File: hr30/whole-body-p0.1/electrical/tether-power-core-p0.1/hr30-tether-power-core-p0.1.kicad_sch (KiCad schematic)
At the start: 0 parts

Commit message: Complete HR-30 safety and clean-build package
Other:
- sheet 03 Two series GV121CAC contactors and feedback loop renamed 03 Two series LC1D40ABD contactors and mirror-feedback loop
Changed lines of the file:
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@@
           (exclude_from_sim no) (in_bom yes) (on_board yes) (dnp no)
           (stroke (width 0.5) (type solid)) (fill (color 0 0 0 0.0000))
-          (property "Sheetname" "03 Two series GV121CAC contactors and feedback loop" (at 284.48 52.16 0) (effects (font (size 1.80 1.80)) (justify left bottom)))
+          (property "Sheetname" "03 Two series LC1D40ABD contactors and mirror-feedback loop" (at 284.48 52.16 0) (effects (font (size 1.80 1.80)) (justify left bottom)))
           (property "Sheetfile" "03_redundant_dc_interruption.kicad_sch" (at 284.48 67.40 0) (effects (font (size 1.50 1.50)) (justify left top)))
           (instances (project "hr30-tether-power-core-p0.1" (path "/ea4c0501-f5a0-52a4-9cf3-7c311b7f38a5" (page "4"))))) (sheet (at 17.78 98.00) (size 116.84 40.64)

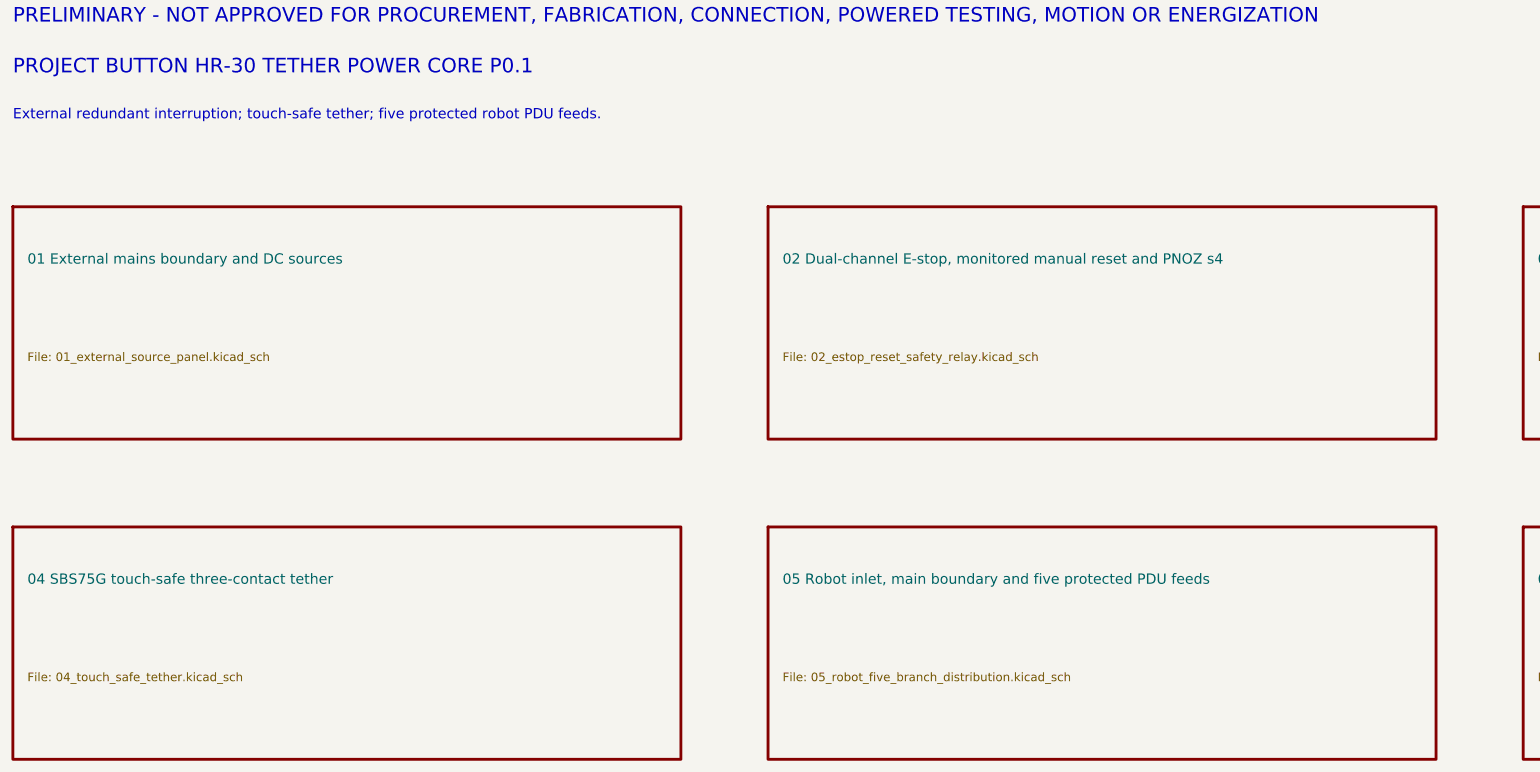
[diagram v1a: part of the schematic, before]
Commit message: Correct HR-30 whole-body power and harness architecture (#48)
Validated whole-body correction; preserves all preliminary and no-energization holds.
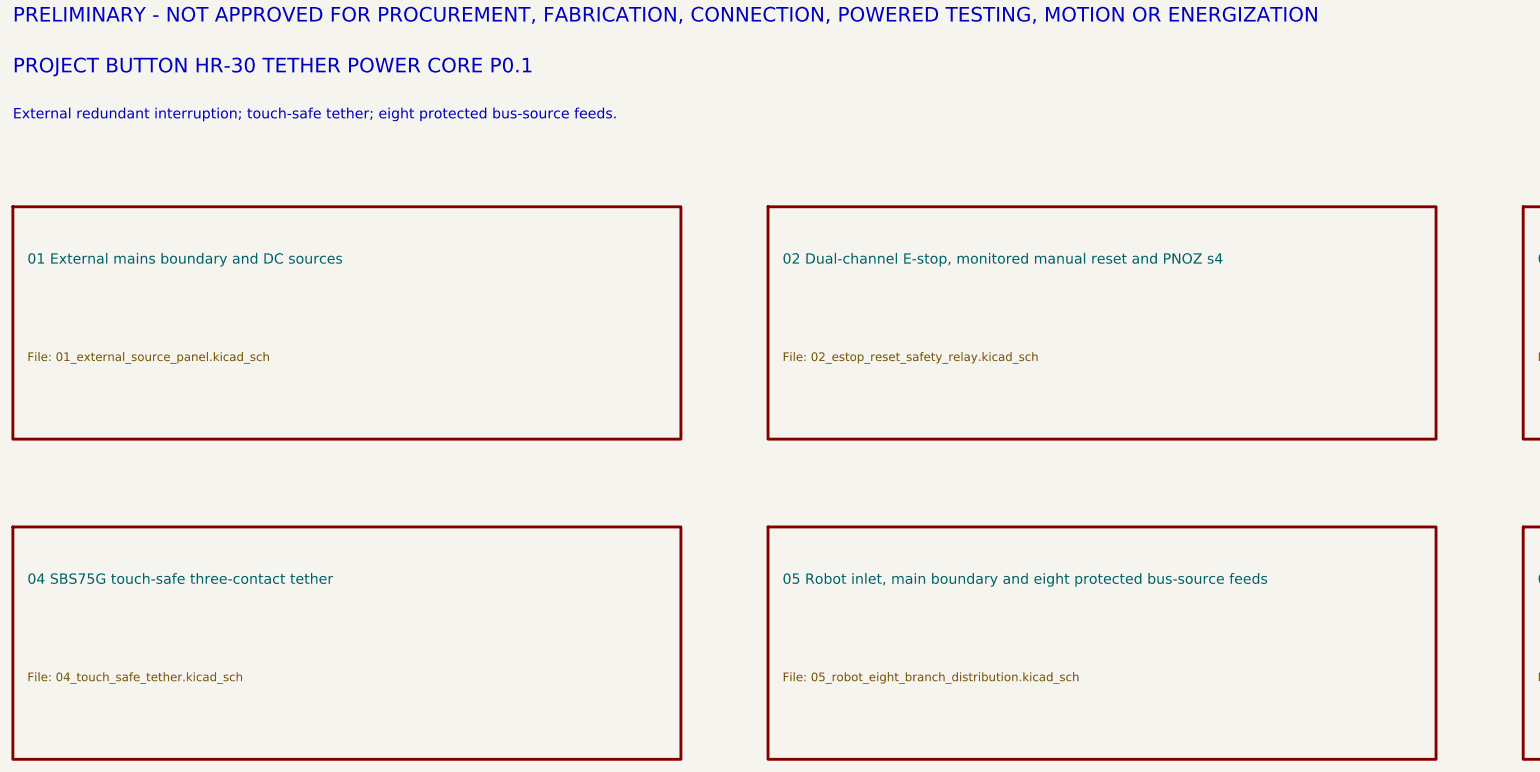
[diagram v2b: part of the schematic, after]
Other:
- removed sheet 05 Robot inlet, main boundary and five protected PDU feeds
- added sheet 05 Robot inlet, main boundary and eight protected bus-source feeds (05_robot_eight_branch_distribution.kicad_sch)
- note added: "External redundant interruption; touch-safe tether; eight protected bus-source feeds."
- note removed: "External redundant interruption; touch-safe tether; five protected robot PDU feeds."
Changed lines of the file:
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@@
   (text "PROJECT BUTTON HR-30 TETHER POWER CORE P0.1" (exclude_from_sim no) (at 17.78 19.05 0)
       (effects (font (size 2.54 2.54)) (justify left bottom)))
-  (text "External redundant interruption; touch-safe tether; five protected robot PDU feeds." (exclude_from_sim no) (at 17.78 27.00 0)
+  (text "External redundant interruption; touch-safe tether; eight protected bus-source feeds." (exclude_from_sim no) (at 17.78 27.00 0)
       (effects (font (size 1.80 1.80)) (justify left bottom)))
   (sheet (at 17.78 42.00) (size 116.84 40.64)
@@
           (exclude_from_sim no) (in_bom yes) (on_board yes) (dnp no)
           (stroke (width 0.5) (type solid)) (fill (color 0 0 0 0.0000))
-          (property "Sheetname" "05 Robot inlet, main boundary and five protected PDU feeds" (at 152.40 108.16 0) (effects (font (size 1.80 1.80)) (justify left bottom)))
-          (property "Sheetfile" "05_robot_five_branch_distribution.kicad_sch" (at 152.40 123.40 0) (effects (font (size 1.50 1.50)) (justify left top)))
+          (property "Sheetname" "05 Robot inlet, main boundary and eight protected bus-source feeds" (at 152.40 108.16 0) (effects (font (size 1.80 1.80)) (justify left bottom)))
+          (property "Sheetfile" "05_robot_eight_branch_distribution.kicad_sch" (at 152.40 123.40 0) (effects (font (size 1.50 1.50)) (justify left top)))
           (instances (project "hr30-tether-power-core-p0.1" (path "/ea4c0501-f5a0-52a4-9cf3-7c311b7f38a5" (page "6"))))) (sheet (at 281.94 98.00) (size 116.84 40.64)
           (exclude_from_sim no) (in_bom yes) (on_board yes) (dnp no)
